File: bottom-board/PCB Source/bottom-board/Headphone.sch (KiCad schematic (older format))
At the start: 23 parts, among them P14 AudioJack3, Q10 J110, Q9 J110, U8 LM4811

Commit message: rev 0.0.3
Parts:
- removed FB11: Ferrite_Bead, Resistor_SMD:R_0603_1608Metric, symbol Device:Ferrite_Bead
- added C85, C86: 100nF, Capacitor_SMD:C_0603_1608Metric, symbol bottom-board-rescue:C_Small
- added D17, D18: BAT54S, Package_TO_SOT_SMD:SOT-23, symbol bottom-board-rescue:BAT54S-Diode
- added R103, R104: 6R8, Resistor_SMD:R_0603_1608Metric, symbol bottom-board-rescue:R_Small-Device
- FB10: symbol Device:Ferrite_Bead -> bottom-board-rescue:Ferrite_Bead-Device
- P14: symbol Connector:AudioJack3 -> bottom-board-rescue:AudioJack3-Connector
- Q10, Q9: value J110 -> BSR58; MPN PMBFJ110,215 -> BSR58
- R90, R91: value 1M -> 1M 1%; symbol Device:R_Small -> bottom-board-rescue:R_Small-Device
- R92, R93, R96, R97: symbol Device:R_Small -> bottom-board-rescue:R_Small-Device
- U8: symbol Amplifier_Audio:LM4811 -> bottom-board-rescue:LM4811-Amplifier_Audio
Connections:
- wire segments 72 -> 91

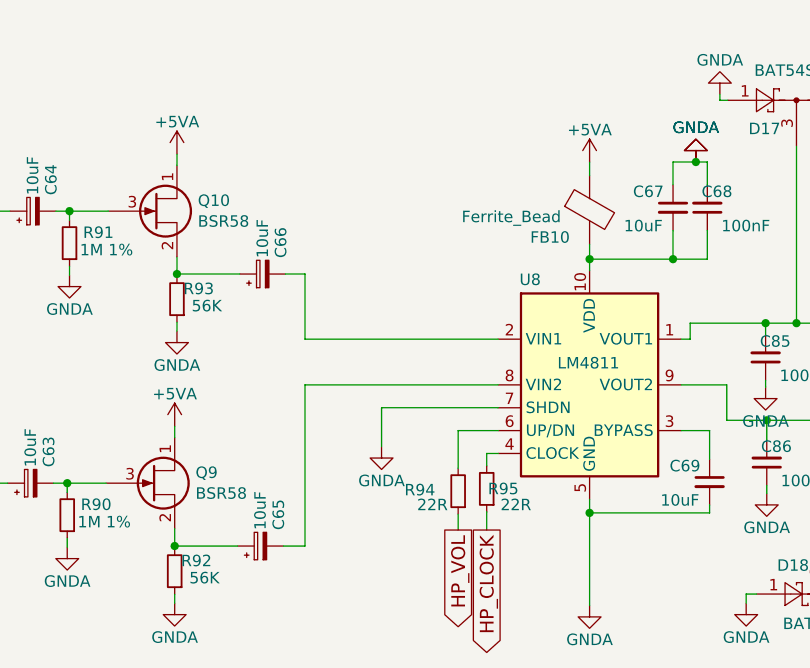
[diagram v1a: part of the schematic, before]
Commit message: change design to 4 layer PCB
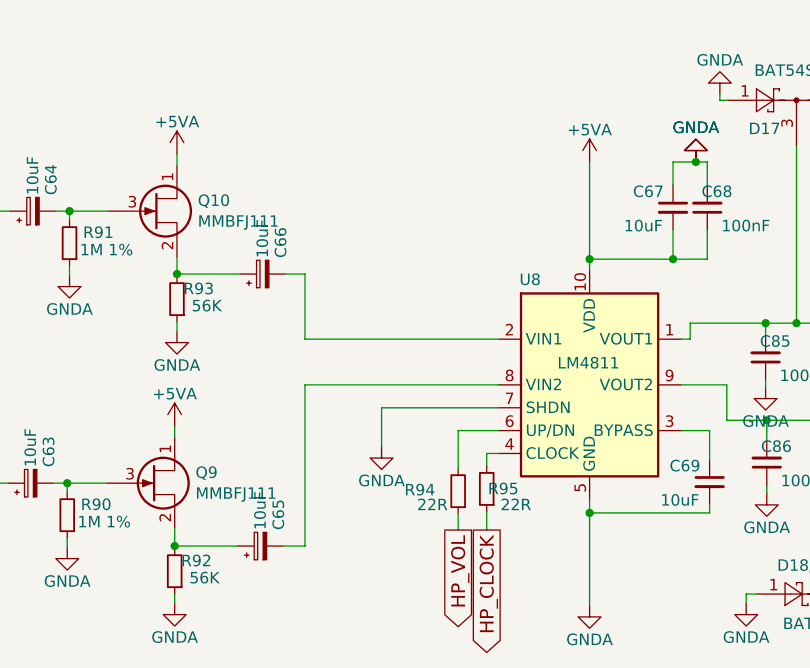
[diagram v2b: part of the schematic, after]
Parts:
- removed FB10: Ferrite_Bead, Resistor_SMD:R_0603_1608Metric, symbol bottom-board-rescue:Ferrite_Bead-Device
- Q10, Q9: value BSR58 -> MMBFJ111; MPN BSR58 -> MMBFJ111
- R103, R104: MPN RR0816P-753-D -> RMCF0603FT6R80
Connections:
- net +5VA: now also C67.2, C68.1, U8.10 (VDD)
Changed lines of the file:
@@
 AR Path="/5F5FD115/5F89CBDC" Ref="Q10"  Part="1"
 F 0 "Q10" H 4056 3071 50  0000 L CNN
-F 1 "BSR58" H 4056 2980 50  0000 L CNN
+F 1 "MMBFJ111" H 4056 2980 50  0000 L CNN
 F 2 "Package_TO_SOT_SMD:SOT-23" H 4065 3125 50  0001 C CNN
 F 3 "" H 3865 3025 50  0001 C CNN
-F 4 "BSR58" H 3865 3025 50  0001 C CNN "MPN"
+F 4 "MMBFJ111" H 3865 3025 50  0001 C CNN "MPN"
 	1    3865 3025
 	1    0    0    -1
@@
 $EndComp
 $Comp
-L bottom-board-rescue:Ferrite_Bead-Device FB?
-U 1 1 5F8B26F8
-P 5770 3020
-AR Path="/54F72B97/5F8B26F8" Ref="FB?"  Part="1"
-AR Path="/5F5FD115/5F8B26F8" Ref="FB10"  Part="1"
-F 0 "FB10" H 5510 2900 50  0000 L CNN
-F 1 "Ferrite_Bead" H 5210 2990 50  0000 L CNN
-F 2 "Resistor_SMD:R_0603_1608Metric" V 5700 3020 50  0001 C CNN
-F 3 "~" H 5770 3020 50  0001 C CNN
-F 4 "BLM18HD102SH1D" H 5770 3020 50  0001 C CNN "MPN"
-	1    5770 3020
-	1    0    0    -1
-$EndComp
-$Comp
 L bottom-board-rescue:GNDA-power #PWR?
 U 1 1 5F8B26FE
@@
 $EndComp
 Wire Wire Line
-	5770 2810 5770 2870
-Wire Wire Line
 	5770 3285 5770 3235
 Wire Wire Line
@@
 	6285 3235 6285 3110
 Connection ~ 5770 3235
-Wire Wire Line
-	5770 3235 5770 3170
 Wire Wire Line
 	6135 3110 6135 3235
@@
 AR Path="/5F5FD115/5F8D33CC" Ref="Q9"  Part="1"
 F 0 "Q9" H 4046 4261 50  0000 L CNN
-F 1 "BSR58" H 4046 4170 50  0000 L CNN
+F 1 "MMBFJ111" H 4046 4170 50  0000 L CNN
 F 2 "Package_TO_SOT_SMD:SOT-23" H 4055 4315 50  0001 C CNN
 F 3 "" H 3855 4215 50  0001 C CNN
-F 4 "BSR58" H 3855 4215 50  0001 C CNN "MPN"
+F 4 "MMBFJ111" H 3855 4215 50  0001 C CNN "MPN"
 	1    3855 4215
 	1    0    0    -1
@@
 F 2 "Resistor_SMD:R_0603_1608Metric" H 7400 3940 50  0001 C CNN
 F 3 "" H 7400 3940 50  0001 C CNN
-F 4 "RR0816P-753-D" V 7400 3940 50  0001 C CNN "MPN"
+F 4 "RMCF0603FT6R80" V 7400 3940 50  0001 C CNN "MPN"
 	1    7400 3940
 	0    -1   -1   0
@@
 F 2 "Resistor_SMD:R_0603_1608Metric" H 7370 3515 50  0001 C CNN
 F 3 "" H 7370 3515 50  0001 C CNN
-F 4 "RR0816P-753-D" V 7370 3515 50  0001 C CNN "MPN"
+F 4 "RMCF0603FT6R80" V 7370 3515 50  0001 C CNN "MPN"
 	1    7370 3515
 	0    1    1    0
@@
 Wire Wire Line
 	7135 4700 7135 4665
+Wire Wire Line
+	5770 2810 5770 3235
 $EndSCHEMATC

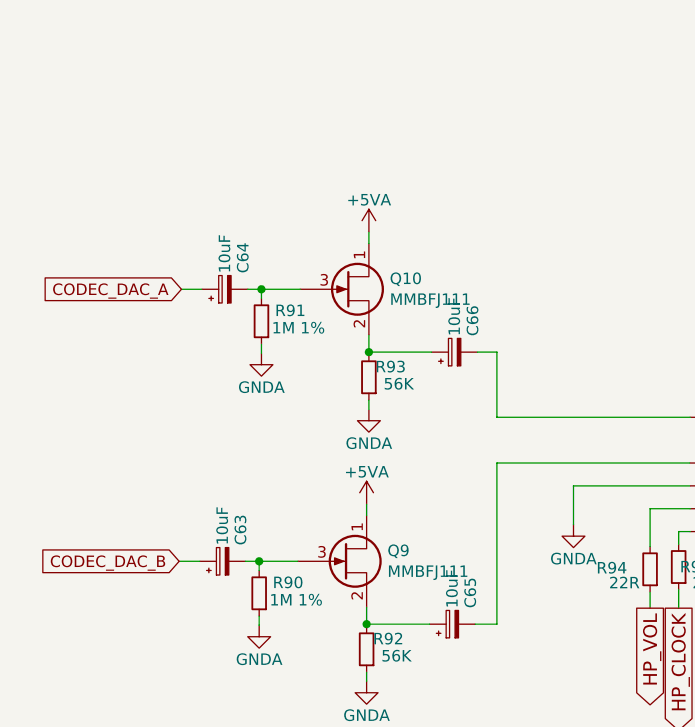
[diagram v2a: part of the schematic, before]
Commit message: change posistion of connectors a tiny bit, now locked in place
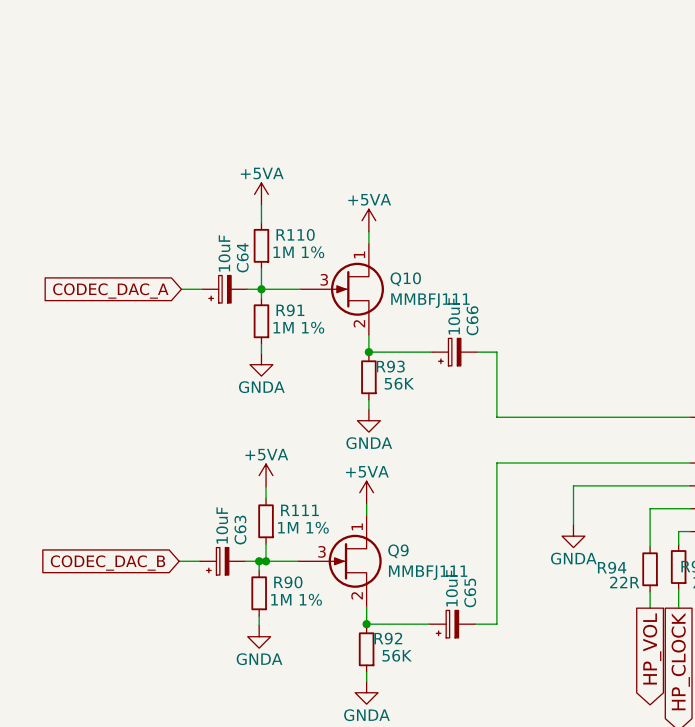
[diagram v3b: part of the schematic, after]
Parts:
- added R110, R111: 1M 1%, Resistor_SMD:R_0603_1608Metric, symbol bottom-board-rescue:R_Small-Device
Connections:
- net +5VA: now also R110.2, R111.2
- net at C64.2, Q10.3 (G), R91.2: now also R110.1
- net at C63.2, Q9.3 (G), R90.2: now also R111.1
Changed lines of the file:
@@
 	3225 4215 3135 4215
 Wire Wire Line
-	3485 4215 3655 4215
+	3485 4215 3515 4215
 Wire Wire Line
 	4430 4490 4525 4490
@@
 Wire Wire Line
 	5770 2810 5770 3235
+$Comp
+L bottom-board-rescue:R_Small-Device R?
+U 1 1 5FC245FB
+P 3495 2835
+AR Path="/54F72C8D/5FC245FB" Ref="R?"  Part="1"
+AR Path="/5F5FD115/5FC245FB" Ref="R110"  Part="1"
+F 0 "R110" H 3436 2789 50  0000 R CNN
+F 1 "1M 1%" H 3450 2865 50  0000 R CNN
+F 2 "Resistor_SMD:R_0603_1608Metric" H 3495 2835 50  0001 C CNN
+F 3 "~" H 3495 2835 50  0001 C CNN
+F 4 "DO NOT PLACE" V 3495 2835 50  0001 C CNN "MPN"
+	1    3495 2835
+	-1   0    0    1
+$EndComp
+$Comp
+L bottom-board-rescue:R_Small-Device R?
+U 1 1 5FC24ED0
+P 3515 4040
+AR Path="/54F72C8D/5FC24ED0" Ref="R?"  Part="1"
+AR Path="/5F5FD115/5FC24ED0" Ref="R111"  Part="1"
+F 0 "R111" H 3456 3994 50  0000 R CNN
+F 1 "1M 1%" H 3470 4070 50  0000 R CNN
+F 2 "Resistor_SMD:R_0603_1608Metric" H 3515 4040 50  0001 C CNN
+F 3 "~" H 3515 4040 50  0001 C CNN
+F 4 "DO NOT PLACE" V 3515 4040 50  0001 C CNN "MPN"
+	1    3515 4040
+	-1   0    0    1
+$EndComp
+$Comp
+L bottom-board-rescue:+5VA-power #PWR?
+U 1 1 5FC254DC
+P 3495 2660
+AR Path="/54F7244B/5FC254DC" Ref="#PWR?"  Part="1"
+AR Path="/5F5FD115/5FC254DC" Ref="#PWR0299"  Part="1"
+F 0 "#PWR0299" H 3495 2510 50  0001 C CNN
+F 1 "+5VA" H 3495 2800 50  0000 C CNN
+F 2 "" H 3495 2660 60  0000 C CNN
+F 3 "" H 3495 2660 60  0000 C CNN
+	1    3495 2660
+	1    0    0    -1
+$EndComp
+$Comp
+L bottom-board-rescue:+5VA-power #PWR?
+U 1 1 5FC267B9
+P 3515 3890
+AR Path="/54F7244B/5FC267B9" Ref="#PWR?"  Part="1"
+AR Path="/5F5FD115/5FC267B9" Ref="#PWR0300"  Part="1"
+F 0 "#PWR0300" H 3515 3740 50  0001 C CNN
+F 1 "+5VA" H 3515 4030 50  0000 C CNN
+F 2 "" H 3515 3890 60  0000 C CNN
+F 3 "" H 3515 3890 60  0000 C CNN
+	1    3515 3890
+	1    0    0    -1
+$EndComp
+Wire Wire Line
+	3515 3890 3515 3940
+Wire Wire Line
+	3515 4140 3515 4215
+Connection ~ 3515 4215
+Wire Wire Line
+	3515 4215 3655 4215
+Wire Wire Line
+	3495 2660 3495 2735
+Wire Wire Line
+	3495 2935 3495 3025
 $EndSCHEMATC

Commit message: cleanup BOM lines
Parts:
- C67, C69: MPN CL10A106MQ8NNNC -> EMK107BBJ106MA-T
- Q10, Q9: value MMBFJ111 -> MMBFJ110; MPN MMBFJ111 -> MMBFJ110
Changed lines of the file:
@@
 encoding utf-8
 Sheet 11 11
-Title ""
-Date ""
-Rev ""
-Comp ""
-Comment1 ""
-Comment2 ""
-Comment3 ""
-Comment4 ""
+Title "MOD Dwarf - Main Board"
+Date "2021-04-07"
+Rev "1.2"
+Comp "MOD Devices GmbH"
+Comment1 "Dwarf Audio processing board"
+Comment2 "https://github.com/moddevices/hw-mod-dwarf"
+Comment3 "Inp Power: 12V 500mA"
+Comment4 "USB outp Power: 500mA"
 $EndDescr
 $Comp
@@
 AR Path="/5F5FD115/5F89CBDC" Ref="Q10"  Part="1"
 F 0 "Q10" H 4056 3071 50  0000 L CNN
-F 1 "MMBFJ111" H 4056 2980 50  0000 L CNN
+F 1 "MMBFJ110" H 4056 2980 50  0000 L CNN
 F 2 "Package_TO_SOT_SMD:SOT-23" H 4065 3125 50  0001 C CNN
 F 3 "" H 3865 3025 50  0001 C CNN
-F 4 "MMBFJ111" H 3865 3025 50  0001 C CNN "MPN"
+F 4 "MMBFJ110" H 3865 3025 50  0001 C CNN "MPN"
 	1    3865 3025
 	1    0    0    -1
@@
 F 2 "Capacitor_SMD:C_0603_1608Metric" H 6135 3010 60  0001 C CNN
 F 3 "" H 6135 3010 60  0000 C CNN
-F 4 "CL10A106MQ8NNNC" H 1685 1310 50  0001 C CNN "MPN"
+F 4 "EMK107BBJ106MA-T" H 1685 1310 50  0001 C CNN "MPN"
 	1    6135 3010
 	1    0    0    -1
@@
 AR Path="/5F5FD115/5F8D33CC" Ref="Q9"  Part="1"
 F 0 "Q9" H 4046 4261 50  0000 L CNN
-F 1 "MMBFJ111" H 4046 4170 50  0000 L CNN
+F 1 "MMBFJ110" H 4046 4170 50  0000 L CNN
 F 2 "Package_TO_SOT_SMD:SOT-23" H 4055 4315 50  0001 C CNN
 F 3 "" H 3855 4215 50  0001 C CNN
-F 4 "MMBFJ111" H 3855 4215 50  0001 C CNN "MPN"
+F 4 "MMBFJ110" H 3855 4215 50  0001 C CNN "MPN"
 	1    3855 4215
 	1    0    0    -1
@@
 F 2 "Capacitor_SMD:C_0603_1608Metric" H 6295 4210 60  0001 C CNN
 F 3 "" H 6295 4210 60  0000 C CNN
-F 4 "CL10A106MQ8NNNC" H 1845 2510 50  0001 C CNN "MPN"
+F 4 "EMK107BBJ106MA-T" H 1845 2510 50  0001 C CNN "MPN"
 	1    6295 4210
 	1    0    0    -1
